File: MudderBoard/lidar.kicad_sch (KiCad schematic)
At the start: 20 parts, among them Q1 N-MOSFET, Q2 N-MOSFET, U1 LM51231QRGRRQ1

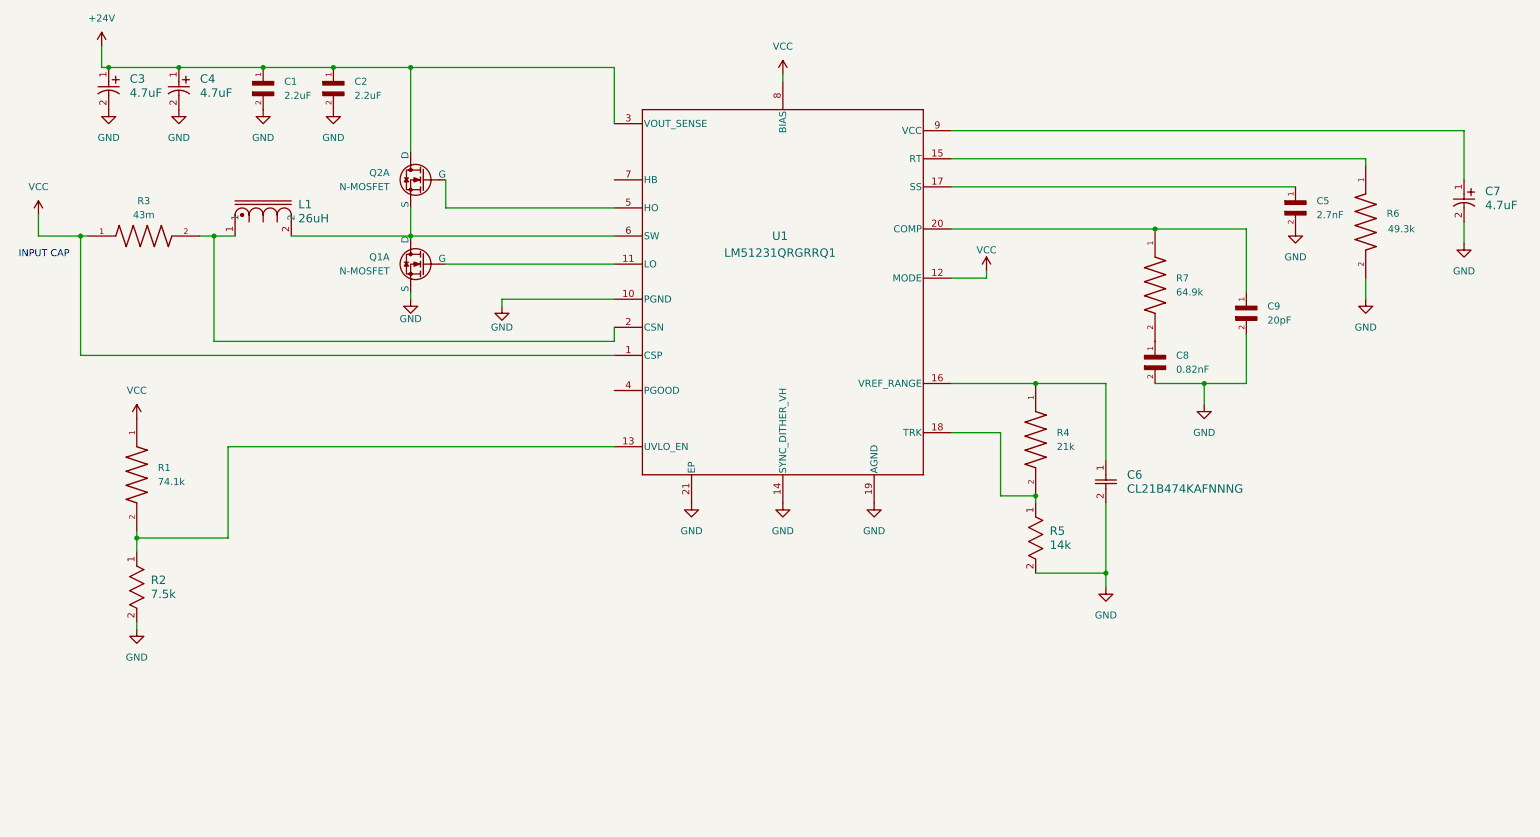
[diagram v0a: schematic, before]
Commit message: Added 24V Boost
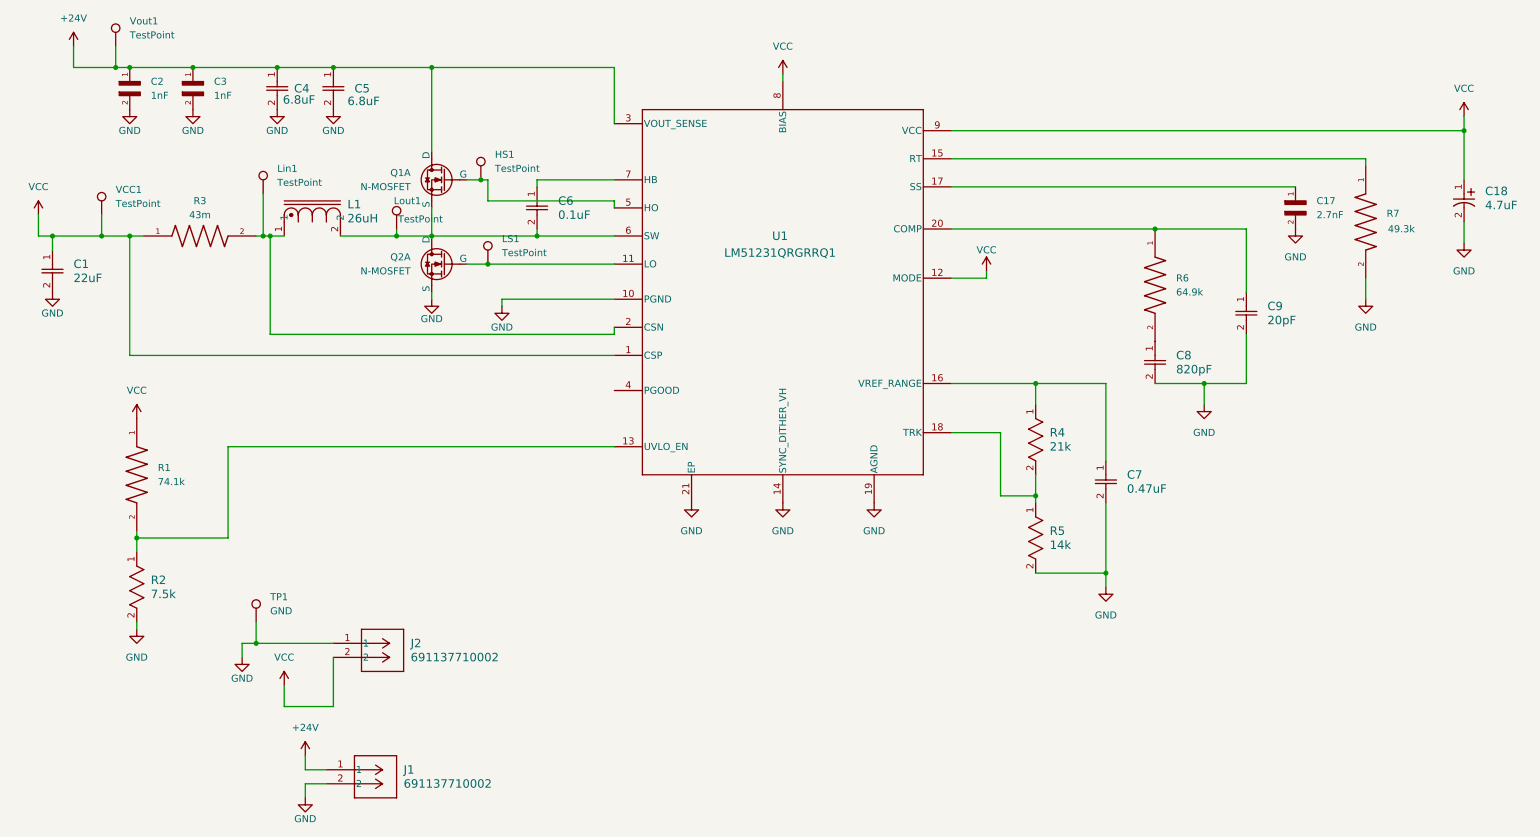
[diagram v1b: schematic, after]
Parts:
- removed C1, C2: 2.2uF, GRM188R6YA225MA12D:CAPC1608X90N, symbol GRM188R6YA225MA12D:GRM188R6YA225MA12D
- removed C3, C4, C7: 4.7uF, TAJB_AVX, symbol TAJB475K035RNJ:TAJB475K035RNJ
- removed C5: 2.7nF, GCM188R71C274KA37D:CAPC1608X90N, symbol GCM188R71C274KA37D:GCM188R71C274KA37D
- removed C6: CL21B474KAFNNNG, CAP_CL_21_SAM, symbol CL21B474KAFNNNG:CL21B474KAFNNNG
- removed C8: 0.82nF, GRM033R71E821KA01D:CAPC0603X33N, symbol GRM033R71E821KA01D:GRM033R71E821KA01D
- removed C9: 20pF, GRM0335C1H200JA01D:CAPC0603X33N, symbol GRM0335C1H200JA01D:GRM0335C1H200JA01D
- removed R4: 21k, RMCF0402FT21K0:RESC1005X35N, symbol RMCF0402FT21K0:RMCF0402FT21K0
- removed R6: 49.3k, RT0603DRE0749K3L:RESC1608X55N, symbol RT0603DRE0749K3L:RT0603DRE0749K3L
- removed R7: 64.9k, RC0603FR-0764K9L:RESC1608X55N, symbol RC0603FR-0764K9L:RC0603FR-0764K9L
- added C1: 22uF, Footprints:CAP_CL_21_SAM, symbol CL21A226MAYNNNE:CL21A226MAYNNNE
- added C17: 2.7nF, Footprints:CAPC1608X90N, symbol GCM188R71C274KA37D:GCM188R71C274KA37D
- added C18: 4.7uF, Footprints:TAJB_AVX, symbol TAJB475K035RNJ:TAJB475K035RNJ
- added C2, C3: 1nF, Footprints:CAPC0603X33N, symbol GRM033R71H102KA12J:GRM033R71H102KA12J
- added C4, C5: 6.8uF, Footprints:CAP_WCAP-ASLI_04p0X05p5_WRE, symbol 865080540003:865080540003
- added C6: 0.1uF, Footprints:CAP_GCJ-18_MUR, symbol GCJ188R72A104KA01D:GCJ188R72A104KA01D
- added C7: 0.47uF, Footprints:CAP_CL_21_SAM, symbol CL21B474KAFNNNG:CL21B474KAFNNNG
- added C8: 820pF, Footprints:CAP_CC0805_YAG, symbol CC0805JRNPO9BN821:CC0805JRNPO9BN821
- added C9: 20pF, Footprints:CAP_CML_0805_.3pF-1500pF_4700pF_STP, symbol CML0805C0G200JT50Vkicad_sym:CML0805C0G200JT50V
- added HS1, LS1, Lin1, Lout1, VCC1, Vout1: TestPoint, TestPoint:TestPoint_THTPad_D1.0mm_Drill0.5mm, symbol Connector:TestPoint
- added J1, J2: 691137710002, Footprints:CONN2_710002_WRE, symbol 691137710002:691137710002
- added R4: 21k, Footprints:RC0805N_YAG, symbol RC0805FR_0721KL:RC0805FR-0721KL
- added R6: 64.9k, Footprints:RESC1608X55N, symbol RC0603FR-0764K9L:RC0603FR-0764K9L
- added R7: 49.3k, Footprints:RESC1608X55N, symbol RT0603DRE0749K3L:RT0603DRE0749K3L
- added TP1: GND, TestPoint:TestPoint_THTPad_D1.0mm_Drill0.5mm, symbol Connector:TestPoint
- L1: footprint SD6030 -> Footprints:SD6030
- Q1, Q2: footprint (none) -> Footprints:P260_QFN5x6_TDSON-8
- R1: footprint RN73R1JTTD7412B25:RESC1608X55N -> Footprints:RESC1608X55N
- R2: footprint RC0603N_YAG -> Footprints:RC0603N_YAG
- R3: footprint RLP73M2BR043JTD:RESC3115X65N -> Footprints:RESC3115X65N
- R5: footprint RC0402N_YAG -> Footprints:RC0402N_YAG
- U1: footprint RGR0020C-IPC_A -> Footprints:RGR0020C-IPC_A
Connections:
- net +24V: now also Q1.3 (D), C2.1, C3.1, C4.1, C5.1, J1.1, Vout1.1; no longer Q2.3 (D)
- net GND: now also Q2.2 (S), C1.2, C17.2, C18.2, C2.2, C3.2, C4.2, C5.2, C7.2, C8.2, C9.2, J1.2, J2.1, R7.2, TP1.1; no longer Q1.2 (S)
- net VCC: now also U1.9 (VCC), C1.1, C18.1, J2.2, VCC1.1
- net at U1.20 (COMP): now also C9.1, R6.1
- net at U1.11 (LO): now also Q2.1 (G), LS1.1; no longer Q1.1 (G)
- net at U1.15 (RT): now also R7.1
- net at U1.16 (VREF_RANGE): now also C7.1, R4.1
- net at U1.17 (SS): now also C17.1
- net at R5.1, U1.18 (TRK): now also R4.2
- net at L1.1, R3.2, U1.2 (CSN): now also Lin1.1
- net at U1.5 (HO): now also Q1.1 (G), HS1.1; no longer Q2.1 (G)
- net at L1.2, U1.6 (SW): now also Q1.2 (S), Q2.3 (D), C6.2, Lout1.1; no longer Q1.3 (D), Q2.2 (S)
- net at U1.7 (HB): now also C6.1
- new net: C8.1, R6.2
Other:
- note removed: "INPUT CAP"

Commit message: Updated Lidar Circuit
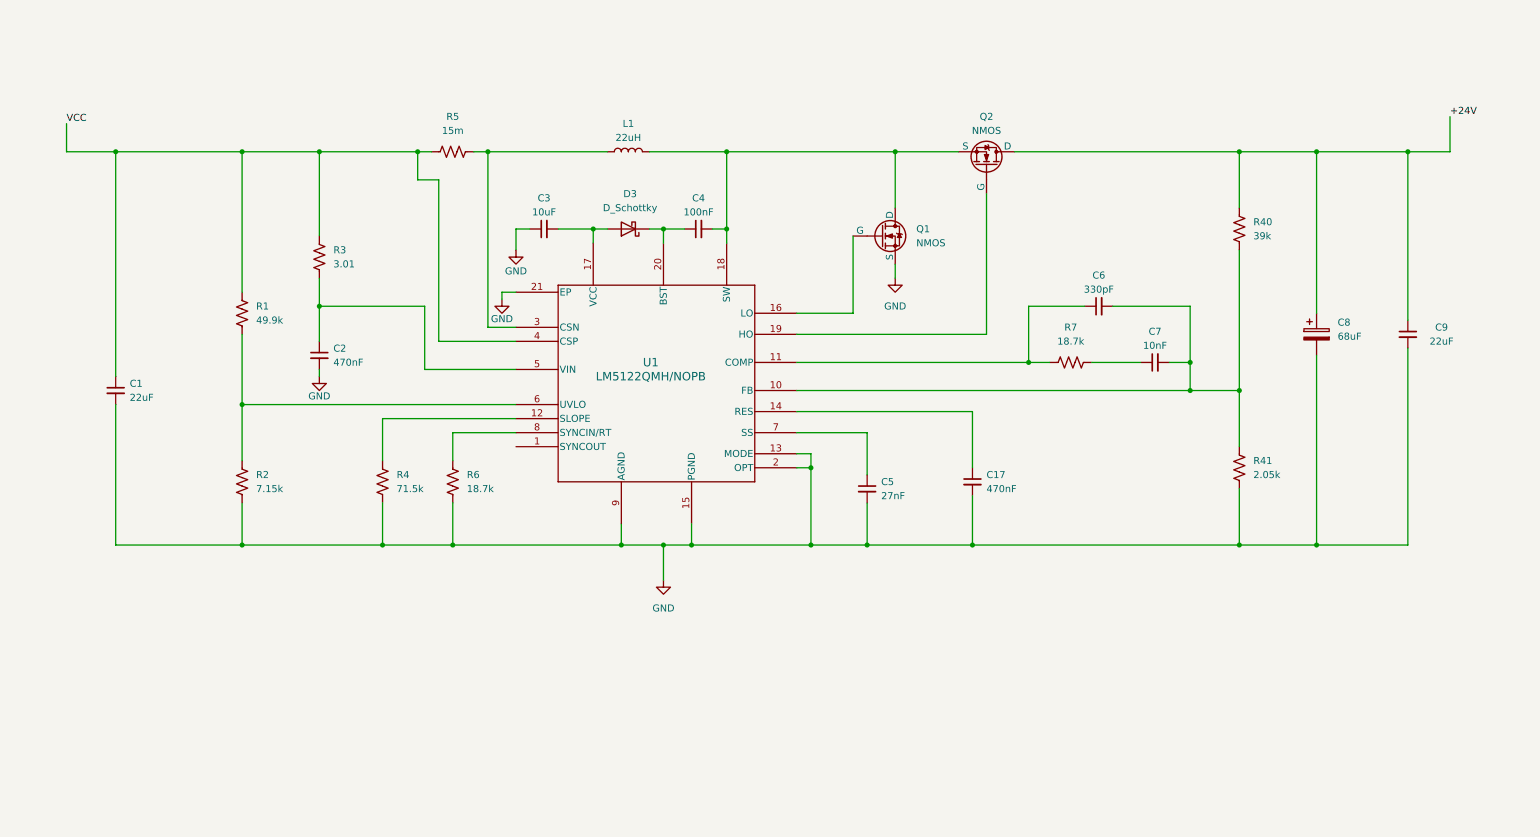
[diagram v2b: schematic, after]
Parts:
- removed C1: 22uF, Footprints:CAP_CL_21_SAM, symbol CL21A226MAYNNNE:CL21A226MAYNNNE
- removed C17: 2.7nF, Footprints:CAPC1608X90N, symbol GCM188R71C274KA37D:GCM188R71C274KA37D
- removed C18: 4.7uF, Footprints:TAJB_AVX, symbol TAJB475K035RNJ:TAJB475K035RNJ
- removed C2, C3: 1nF, Footprints:CAPC0603X33N, symbol GRM033R71H102KA12J:GRM033R71H102KA12J
- removed C4, C5: 6.8uF, Footprints:CAP_WCAP-ASLI_04p0X05p5_WRE, symbol 865080540003:865080540003
- removed C6: 0.1uF, Footprints:CAP_GCJ-18_MUR, symbol GCJ188R72A104KA01D:GCJ188R72A104KA01D
- removed C7: 0.47uF, Footprints:CAP_CL_21_SAM, symbol CL21B474KAFNNNG:CL21B474KAFNNNG
- removed C8: 820pF, Footprints:CAP_CC0805_YAG, symbol CC0805JRNPO9BN821:CC0805JRNPO9BN821
- removed C9: 20pF, Footprints:CAP_CML_0805_.3pF-1500pF_4700pF_STP, symbol CML0805C0G200JT50Vkicad_sym:CML0805C0G200JT50V
- removed HS1, LS1, Lin1, Lout1, VCC1, Vout1: TestPoint, TestPoint:TestPoint_THTPad_D1.0mm_Drill0.5mm, symbol Connector:TestPoint
- removed J1, J2: 691137710002, Footprints:CONN2_710002_WRE, symbol 691137710002:691137710002
- removed L1: 26uH, Footprints:SD6030, symbol SD6030_270_R:SD6030-270-R
- removed Q1, Q2: N-MOSFET, Footprints:P260_QFN5x6_TDSON-8, symbol DI110N04PQ-AQ:nMOS
- removed R1: 74.1k, Footprints:RESC1608X55N, symbol RN73R1JTTD7412B25:RN73R1JTTD7412B25
- removed R2: 7.5k, Footprints:RC0603N_YAG, symbol RC0603FR_077K5L:RC0603FR-077K5L
- removed R3: 43m, Footprints:RESC3115X65N, symbol RLP73M2BR043JTD:RLP73M2BR043JTD
- removed R4: 21k, Footprints:RC0805N_YAG, symbol RC0805FR_0721KL:RC0805FR-0721KL
- removed R5: 14k, Footprints:RC0402N_YAG, symbol RC0402FR-0714KL:RC0402FR-0714KL
- removed R6: 64.9k, Footprints:RESC1608X55N, symbol RC0603FR-0764K9L:RC0603FR-0764K9L
- removed R7: 49.3k, Footprints:RESC1608X55N, symbol RT0603DRE0749K3L:RT0603DRE0749K3L
- removed TP1: GND, TestPoint:TestPoint_THTPad_D1.0mm_Drill0.5mm, symbol Connector:TestPoint
- removed U1: LM51231QRGRRQ1, Footprints:RGR0020C-IPC_A, symbol LM51231QRGRRQ1:LM51231QRGRRQ1
- added C1, C9: 22uF, symbol Device:C_Small
- added C17, C2: 470nF, symbol Device:C_Small
- added C3: 10uF, symbol Device:C_Small
- added C4: 100nF, symbol Device:C_Small
- added C5: 27nF, symbol Device:C_Small
- added C6: 330pF, symbol Device:C_Small
- added C7: 10nF, symbol Device:C_Small
- added C8: 68uF, symbol Device:C_Polarized
- added D3: D_Schottky, symbol Device:D_Schottky
- added L1: 22uH, symbol Device:L
- added Q1, Q2: NMOS, symbol Simulation_SPICE:NMOS
- added R1: 49.9k, symbol Device:R_US
- added R2: 7.15k, symbol Device:R_US
- added R3: 3.01, symbol Device:R_US
- added R4: 71.5k, symbol Device:R_US
- added R40: 39k, symbol Device:R_US
- added R41: 2.05k, symbol Device:R_US
- added R5: 15m, symbol Device:R_US
- added R6, R7: 18.7k, symbol Device:R_US
- added U1: LM5122QMH/NOPB, HTSSOP20, symbol LM5122H:LM5122QMH_NOPB
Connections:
- net +24V: now also C8.1, C9.1, Q2.1 (D), R40.1
- net GND: now also C1.2, C17.2, C2.2, C3.1, C5.2, C8.2, C9.2, Q1.3 (S), R2.2, R4.2, R41.2, R6.2, U1.13 (MODE), U1.15 (PGND), U1.2 (OPT), U1.21 (EP), U1.9 (AGND)
- net VCC: now also C1.1, R1.1, R3.1, R5.1, U1.4 (CSP)
- new net: C6.2, C7.2, R40.2, R41.1, U1.10 (FB)
- new net: R6.1, U1.8 (SYNCIN/RT)
- new net: C5.1, U1.7 (SS)
- new net: R4.1, U1.12 (SLOPE)
- new net: Q2.2 (G), U1.19 (HO)
- new net: C4.2, L1.2, Q1.1 (D), Q2.3 (S), U1.18 (SW)
- new net: C2.1, R3.2, U1.5 (VIN)
- new net: C6.1, R7.2, U1.11 (COMP)
- new net: C17.1, U1.14 (RES)
- new net: Q1.2 (G), U1.16 (LO)
- new net: C3.2, D3.2 (A), U1.17 (VCC)
- new net: C4.1, D3.1 (K), U1.20 (BST)
- new net: L1.1, R5.2, U1.3 (CSN)
- new net: R1.2, R2.1, U1.6 (UVLO)
- new net: C7.1, R7.1

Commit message: added jetson circuit
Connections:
- net VCC renamed +BATT
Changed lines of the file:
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@@
 		)
 	)
-	(label "VCC"
+	(label "+BATT"
 		(at 21.59 44.45 0)
 		(fields_autoplaced yes)

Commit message: downloaded footprints for Lidar
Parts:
- L1: footprint (none) -> Lidar_Foot:IND_SRR1210-220M
- Q1, Q2: footprint (none) -> Lidar_Foot:TRANS_CSD17571Q2
- U1: footprint HTSSOP20 -> Lidar_Foot:SOP65P640X110-21N
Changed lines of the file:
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@@
 			)
 		)
-		(property "Footprint" ""
+		(property "Footprint" "Lidar_Foot:TRANS_CSD17571Q2"
 			(at 190.5 46.99 0)
 			(effects
@@
 			)
 		)
-		(property "Footprint" "HTSSOP20"
+		(property "Footprint" "Lidar_Foot:SOP65P640X110-21N"
 			(at 131.318 53.086 0)
 			(effects
@@
 			)
 		)
-		(property "Footprint" ""
+		(property "Footprint" "Lidar_Foot:IND_SRR1210-220M"
 			(at 123.19 49.53 0)
 			(effects
@@
 			)
 		)
-		(property "Footprint" ""
+		(property "Footprint" "Lidar_Foot:TRANS_CSD17571Q2"
 			(at 173.99 62.23 0)
 			(effects
